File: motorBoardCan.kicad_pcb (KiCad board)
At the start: 6 copper layers, 50 x 50 mm, 47 parts, among them J1 Conn_01x04_Pin, J2 Conn_01x04_Pin, J3 Conn_02x04_Top_Bottom, J4 Conn_01x02_Pin, J5 Conn_01x02_Pin, J6 Conn_02x04_Top_Bottom, J7 Conn_01x02_Pin, J8 Conn_01x02_Pin, U1 NUCLEO-G431KB, U10 TPS563200, U4 SN65HVD230, U5 LD1117S33TR_SOT223

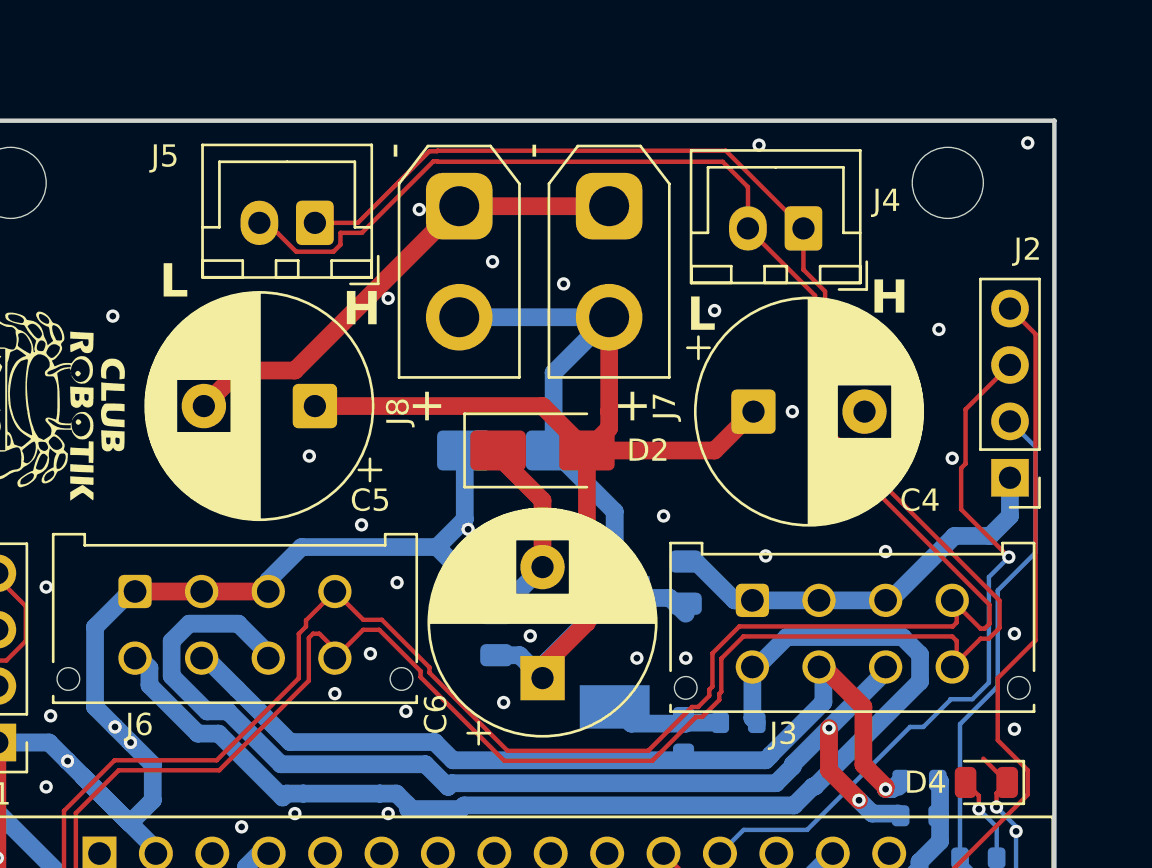
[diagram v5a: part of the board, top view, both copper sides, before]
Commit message: move capacitors for easier access to main bus connectors + add 24V flood fill
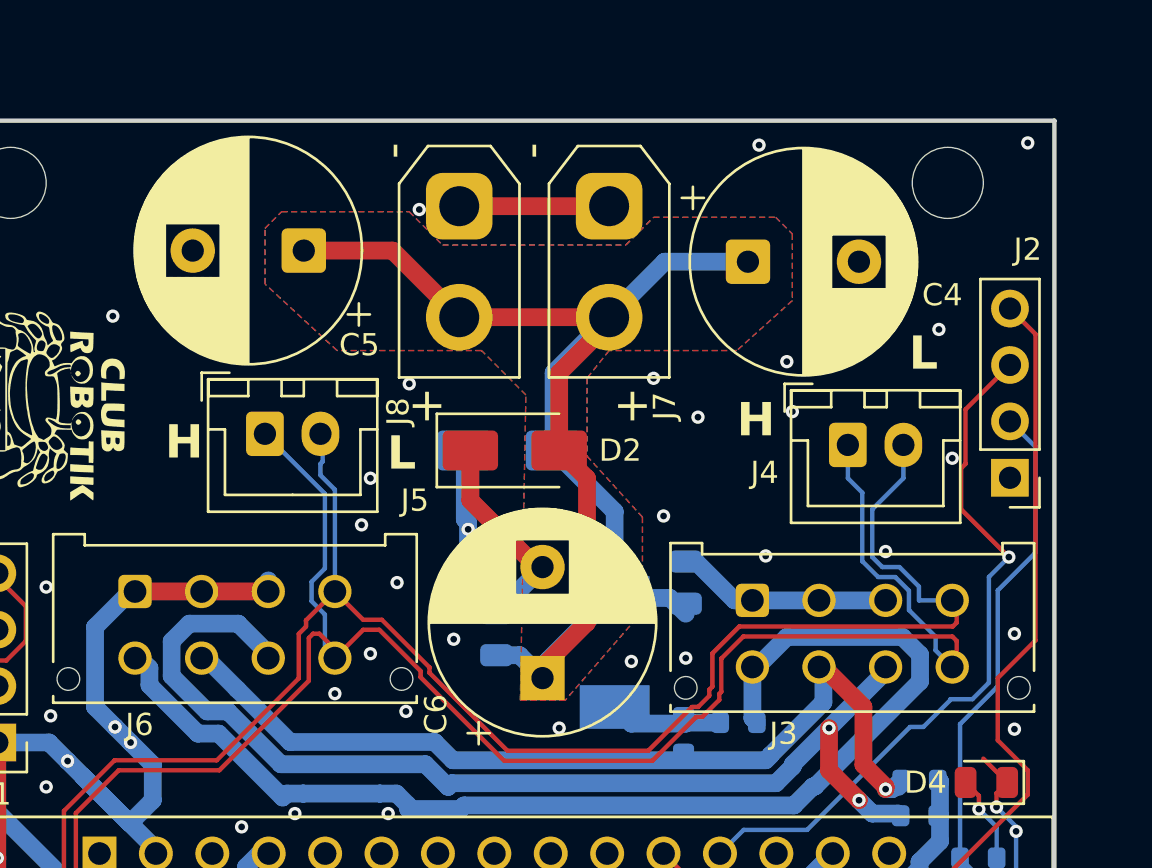
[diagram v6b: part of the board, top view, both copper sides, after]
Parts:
- moved J4 9.95 mm to (117.5, 72.0), turned to 0 degrees
- moved J5 9.76 mm to (91.2, 71.5), turned to 0 degrees
- moved C5 7.02 mm to (93.0, 63.2)
- moved C4 6.75 mm to (113.0, 63.8)
- moved D2 1.25 mm to (102.5, 72.2)
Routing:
- net CAN-: track 115.9 -> 82.3 mm
- net GND: track 208.2 -> 175.5 mm
- net CAN+: track 112.8 -> 87.8 mm
- net 24V: track 71.9 -> 67.2 mm
- added copper zone on B.Cu, net 24V
- added copper zone on F.Cu, net 24V

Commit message: various updates
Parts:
- removed C4: C_Polarized, Capacitor_THT:CP_Radial_D10.0mm_P5.00mm
- added C8: 10uF, Capacitor_SMD:C_0805_2012Metric, B.Cu at (91.7, 75.9)
- added D5: 14V, Diode_SMD:D_SOD-123, B.Cu at (97.5, 72.3)
- added D6: D_transistor, Diode_SMD:D_SOD-123, B.Cu at (91.1, 61.2)
- added D7: D_transistor, Diode_SMD:D_SOD-123, B.Cu at (82.4, 72.3)
- added D8: D_transistor, Diode_SMD:D_SOD-123, B.Cu at (83.1, 63.8)
- added D9: D_transistor, Diode_SMD:D_SOD-123, B.Cu at (97.2, 69.2)
- added F2: Fuse, Fuse:Fuse_Littelfuse-NANO2-451_453, B.Cu at (97.4, 77.8)
- added J10: Conn_01x02_Pin, Connector_JST:JST_XH_B2B-XH-A_1x02_P2.50mm_Vertical, F.Cu at (93.5, 63.8)
- added J11: Conn_01x02_Pin, Connector_JST:JST_XH_B2B-XH-A_1x02_P2.50mm_Vertical, F.Cu at (86.7, 63.8)
- added J12: Conn_01x02_Pin, Connector_JST:JST_XH_B2B-XH-A_1x02_P2.50mm_Vertical, F.Cu at (93.5, 72.2)
- added J9: Conn_01x02_Pin, Connector_JST:JST_XH_B2B-XH-A_1x02_P2.50mm_Vertical, F.Cu at (86.7, 72.2)
- added Q1: AO3400A, Package_TO_SOT_SMD:SOT-23, B.Cu at (82.6, 75.1)
- added Q2: AO3400A, Package_TO_SOT_SMD:SOT-23, B.Cu at (96.6, 60.8)
- added Q3: AO3400A, Package_TO_SOT_SMD:SOT-23, B.Cu at (83.2, 66.6)
- added Q4: AO3400A, Package_TO_SOT_SMD:SOT-23, B.Cu at (94.2, 66.7)
- added R20: 220R, Resistor_SMD:R_0603_1608Metric, B.Cu at (82.5, 78.4)
- added R3: 220R, Resistor_SMD:R_0603_1608Metric, B.Cu at (94.0, 59.4)
- added R5: 220R, Resistor_SMD:R_0603_1608Metric, B.Cu at (83.8, 70.4)
- added R9: 220R, Resistor_SMD:R_0603_1608Metric, B.Cu at (91.0, 65.5)
- added U2: XGZP160-SOP_pressure_sensor, LibraryVictor2026:XGZP160-SOP, F.Cu at (80.2, 68.9)
- added U3: XGZP160-SOP_pressure_sensor, LibraryVictor2026:XGZP160-SOP, F.Cu at (115.8, 64.0)
- C5: footprint Capacitor_THT:CP_Radial_D10.0mm_P5.00mm -> Capacitor_THT:CP_Radial_D8.0mm_P3.50mm
- D1: footprint Capacitor_SMD:C_0805_2012Metric -> Diode_SMD:D_SOD-123
- J1, J2: footprint Connector_PinHeader_2.54mm:PinHeader_1x04_P2.54mm_Vertical -> Connector_JST:JST_XH_B4B-XH-A_1x04_P2.50mm_Vertical
- moved G*** 37.1 mm to (119.1, 65.5)
- moved J5 27.2 mm to (118.4, 73.0), turned to 90 degrees
- moved C5 21.3 mm to (114.2, 64.5), turned to 90 degrees
- moved J4 7.50 mm to (110.0, 72.0)
- moved J1 7.44 mm to (78.7, 78.0), turned to -90 degrees
- moved G*** 1.13 mm to (80.8, 71.1)
- moved J2 0.67 mm to (124.5, 72.9), turned to 90 degrees
- moved J8 0.58 mm to (100.5, 61.0)
- moved J7 0.25 mm to (106.8, 61.0)
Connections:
- U1 pad 3_6: /BRAKE_B -> /Trans_0
- U1 pad 3_7: unconnected-(U1A-PB7-Pad3_7) -> /Trans_3
- U1 pad 3_8: unconnected-(U1A-PA15-Pad3_8) -> /Trans_1
- U1 pad 3_9: unconnected-(U1A-PB6-Pad3_9) -> /Trans_2
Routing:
- net /Trans_1: track 0.00 -> 67.8 mm, vias 0 -> 1
- net /Trans_3: track 0.00 -> 59.0 mm, vias 0 -> 1
- net /Trans_2: track 0.00 -> 55.8 mm, vias 0 -> 1
- net 12V: track 0.00 -> 45.4 mm, vias 0 -> 9
- net /Trans_0: track 0.00 -> 39.8 mm, vias 0 -> 1
- net GND: track 175.5 -> 157.7 mm, vias 69 -> 75
- net Net-(D9-K): track 0.00 -> 12.3 mm
- net /ENC1_B: track 33.9 -> 24.2 mm
- net 24V: track 67.2 -> 59.0 mm, vias 0 -> 4
- net Net-(D6-K): track 0.00 -> 7.73 mm
- net 12V_POW_P: track 40.5 -> 46.3 mm
- net Net-(D7-K): track 0.00 -> 5.76 mm
- net Net-(D8-K): track 0.00 -> 5.10 mm
- net Net-(Q3-G): track 0.00 -> 4.82 mm
- net Net-(Q2-G): track 0.00 -> 2.89 mm
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- added copper zone on B.Cu, net 12V
- added copper zone on F.Cu, net 12V
- added copper zone on In3.Cu, net 12V
- added copper zone on In3.Cu, net 24V
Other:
- outline, holes or cut-outs redrawn
- board text added: "24P 12P 12E CAN+"
- board text added: "4x Trans 12V"

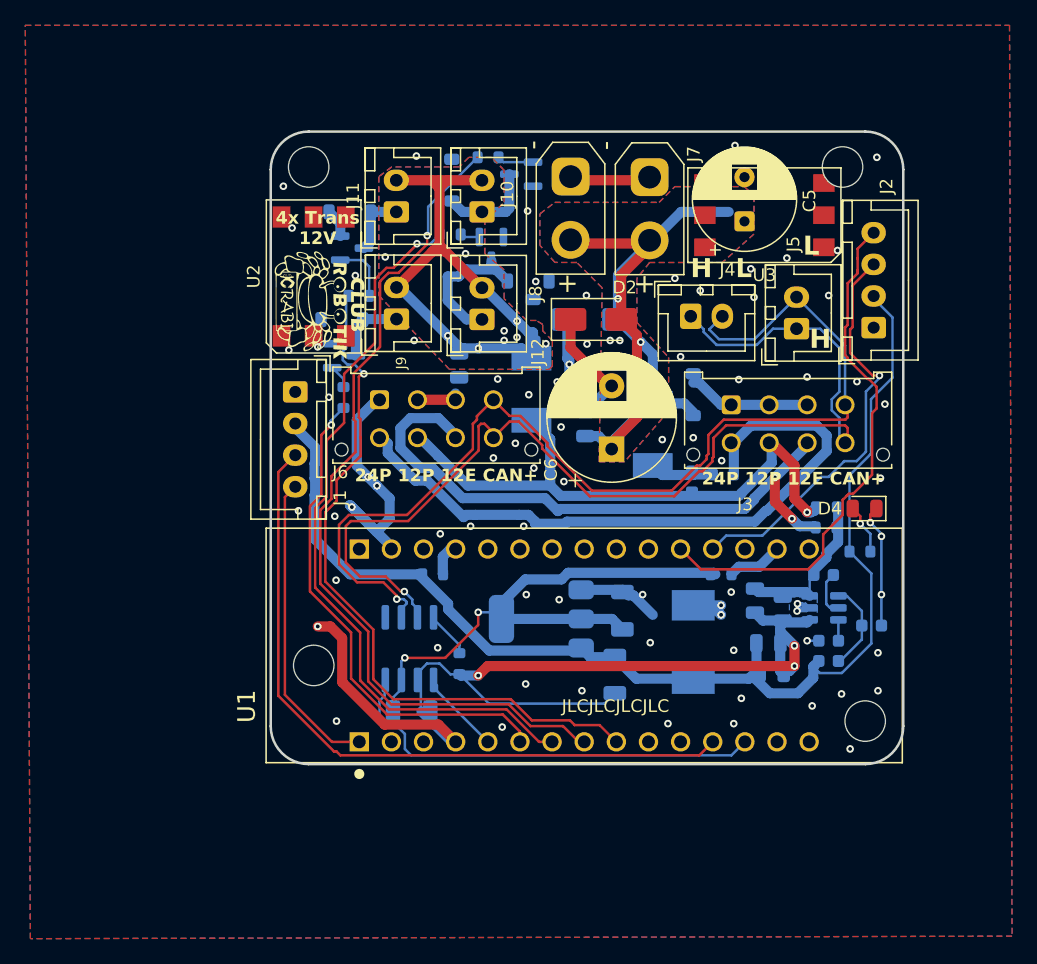
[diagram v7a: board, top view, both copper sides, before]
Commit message: remove pressure measure, add voltage measure, re-route
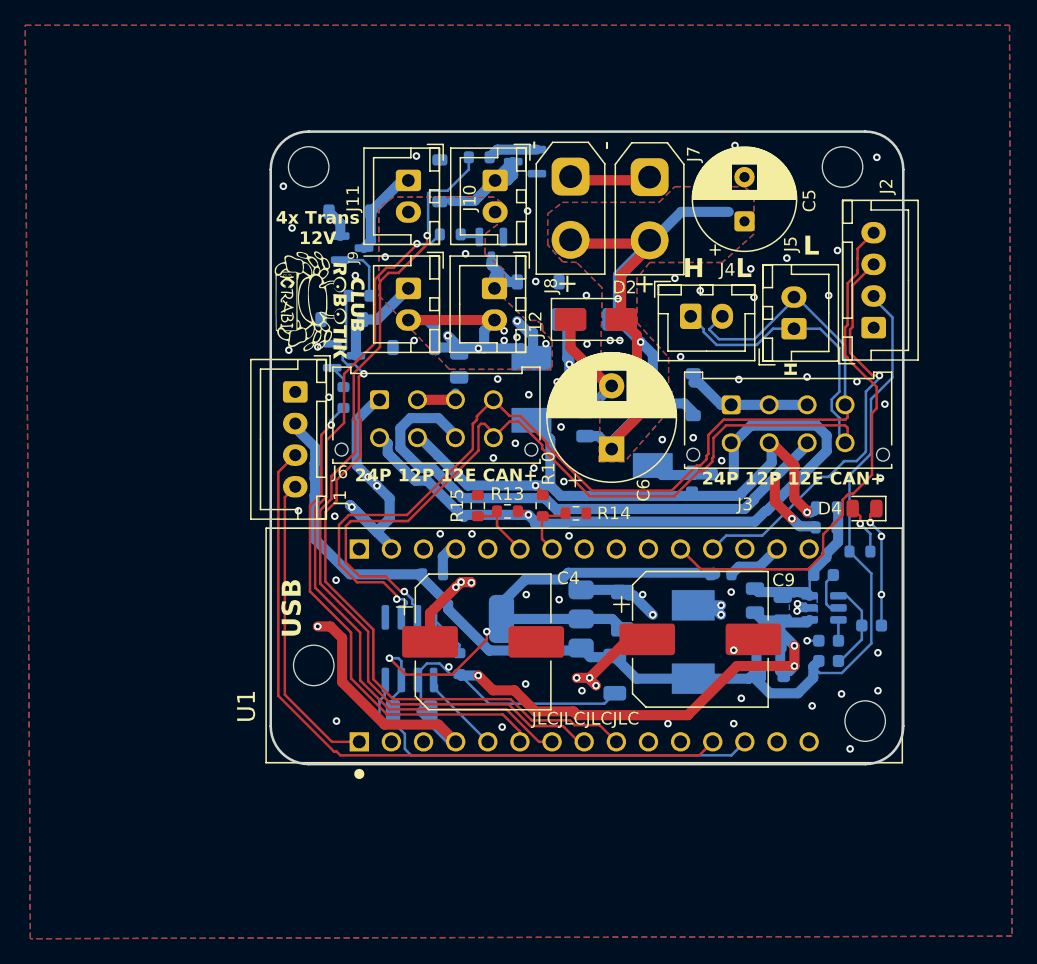
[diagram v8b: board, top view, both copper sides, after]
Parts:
- removed U2, U3: XGZP160-SOP_pressure_sensor, LibraryVictor2026:XGZP160-SOP
- added C4: C_Polarized, Capacitor_SMD:CP_Elec_10x10.5, F.Cu at (93.6, 97.7)
- added C9: C_Polarized, Capacitor_SMD:CP_Elec_10x10.5, F.Cu at (110.8, 97.5)
- added R10: 88kR, Resistor_SMD:R_0603_1608Metric, F.Cu at (98.3, 87.0)
- added R13: 88kR, Resistor_SMD:R_0603_1608Metric, F.Cu at (95.5, 87.4)
- added R14: 10kR, Resistor_SMD:R_0603_1608Metric, F.Cu at (100.9, 87.6)
- added R15: 5kR, Resistor_SMD:R_0603_1608Metric, F.Cu at (93.2, 87.0)
- R11: value DNP -> 0R
- R12: value 0R -> DNP
- moved D5 9.66 mm to (88.1, 74.5), turned to 180 degrees
- moved J10 2.69 mm to (94.5, 61.3), turned to -90 degrees
- moved J11 2.66 mm to (87.7, 61.3), turned to -90 degrees
- moved J12 2.64 mm to (94.5, 69.8), turned to -90 degrees
- moved J9 2.60 mm to (87.7, 69.8), turned to -90 degrees
- moved Q2 1.04 mm to (96.9, 59.8)
- moved D6 0.94 mm to (90.2, 61.3)
- moved D9 0.79 mm to (97.9, 69.3)
- moved R3 0.70 mm to (93.3, 59.4)
- moved J5 0.20 mm to (118.2, 73.0)
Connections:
- U1 pad 4_6: /CURRENT_B -> /24V_measure
- U1 pad 4_7: /CURRENT_A -> /12V_measure
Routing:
- net 12V: track 45.4 -> 27.2 mm
- net 24V_POW_P: track 53.6 -> 62.2 mm, vias 0 -> 4
- net 12V_POW_P: track 46.3 -> 53.9 mm, vias 1 -> 5
- net Net-(D9-K): track 12.3 -> 5.68 mm
- net /24V_measure: track 0.00 -> 5.40 mm
- net /12V_measure: track 0.00 -> 4.80 mm
- net GND: track 157.7 -> 160.6 mm
- net 3.3V: track 43.9 -> 46.0 mm
- net Net-(D7-K): track 5.76 -> 7.76 mm
- net Net-(D8-K): track 5.10 -> 7.08 mm
- net Net-(Q2-G): track 2.89 -> 3.99 mm
- net Net-(D6-K): track 7.73 -> 8.77 mm
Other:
- board text added: "USB"
